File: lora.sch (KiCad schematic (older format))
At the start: 52 parts, among them J11 Conn_Coaxial, J2 Humidity, J3 Temp, J5 Temp, J6 VDD, J7 GPS, J8 SIM800, J9 I2C, Q1 AO3401A, Q2 AO3401A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

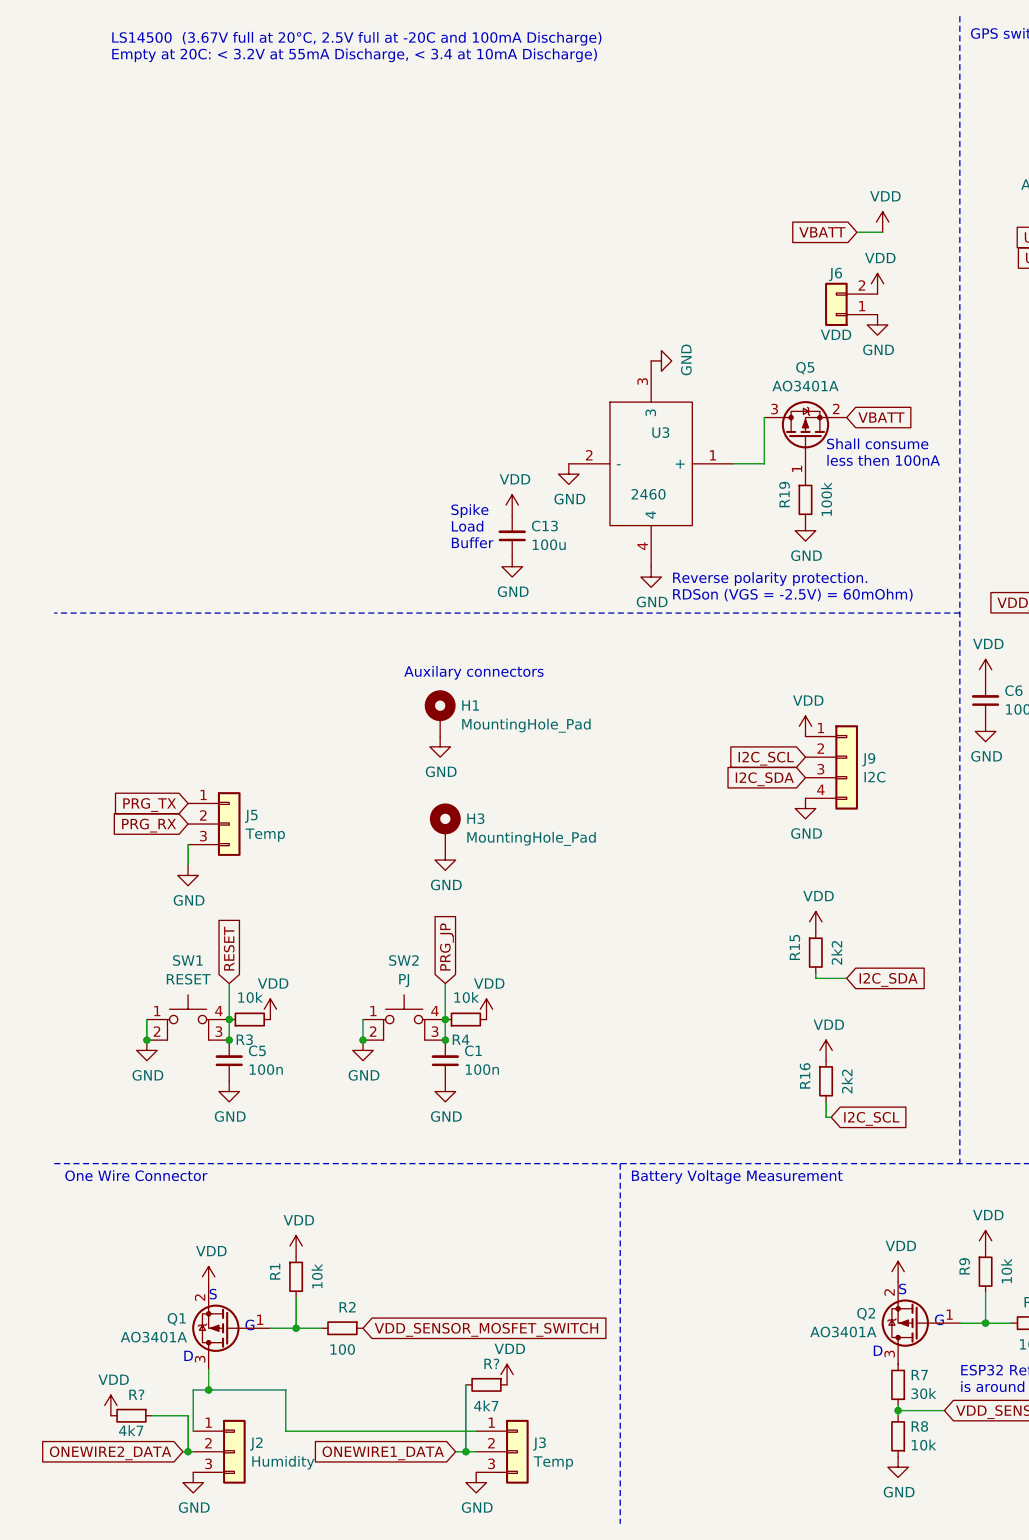
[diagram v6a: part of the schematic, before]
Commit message: updated part number step up
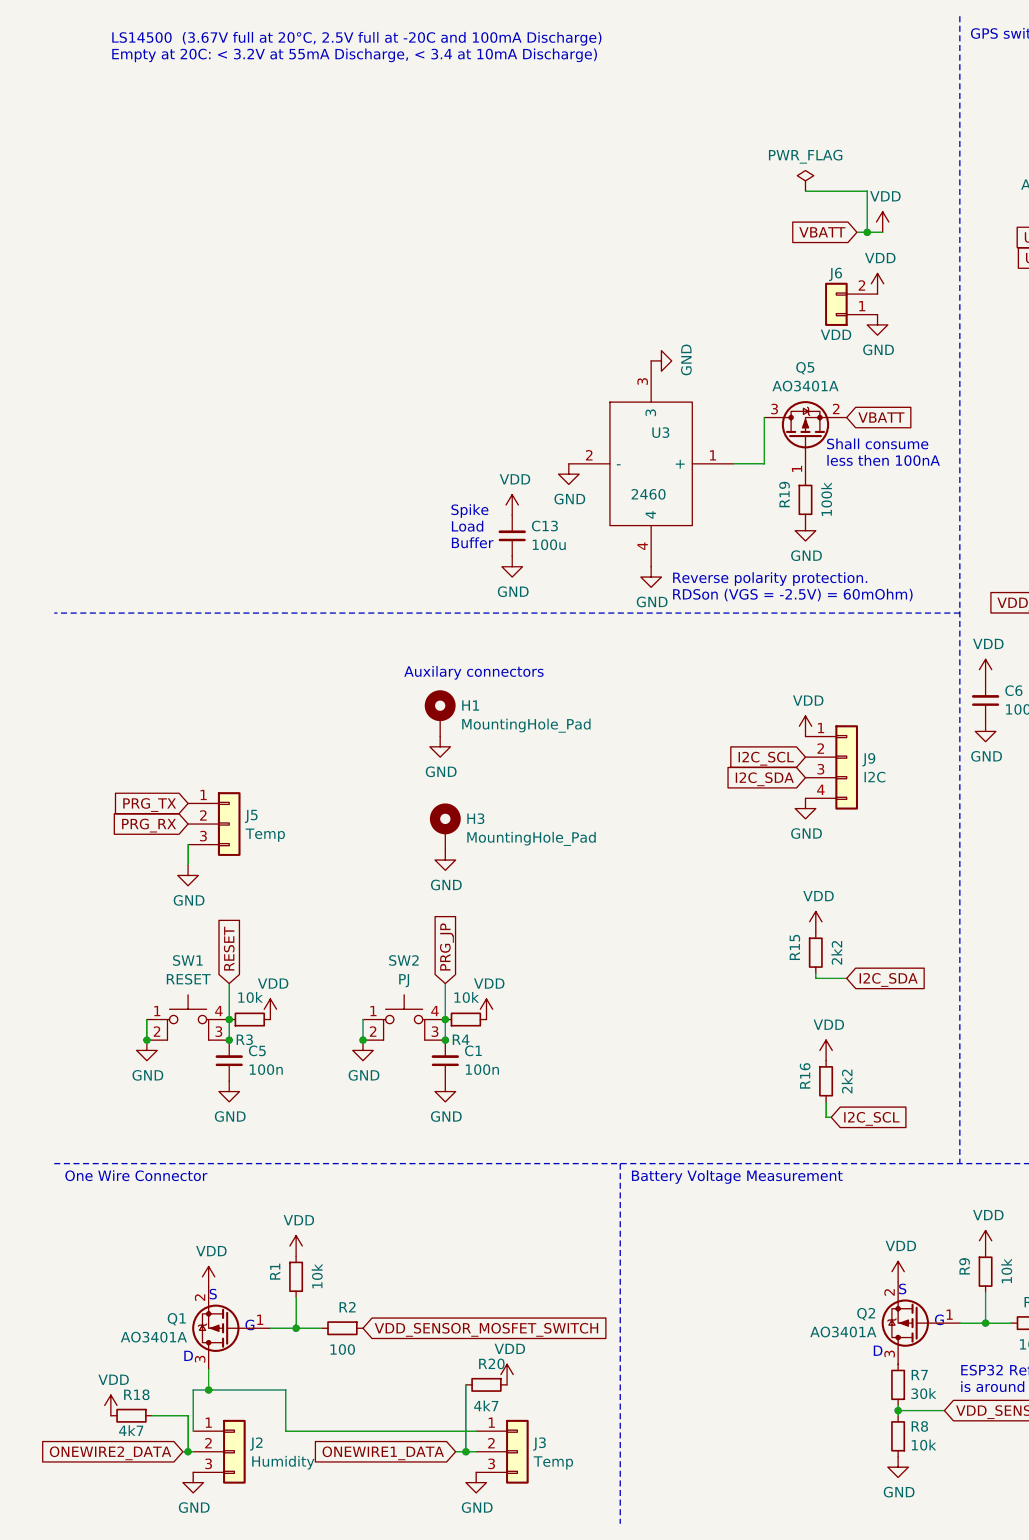
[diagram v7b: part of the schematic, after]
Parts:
- gave numbers to parts that had none: 2
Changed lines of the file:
@@
 $EndComp
 Wire Wire Line
-	4375 1525 4500 1525
+	4375 1525 4425 1525
 Wire Notes Line
 	3225 6050 3225 7800
@@
 	8350 3675 8550 3675
 $Comp
-L Device:R_Small R?
+L Device:R_Small R20
 U 1 1 614025B8
 P 2575 7125
-F 0 "R?" V 2475 7150 50  0000 C CNN
+F 0 "R20" V 2475 7150 50  0000 C CNN
 F 1 "4k7" V 2680 7125 50  0000 C CNN
 F 2 "Capacitor_SMD:C_0603_1608Metric" H 2575 7125 50  0001 C CNN
@@
 $EndComp
 $Comp
-L Device:R_Small R?
+L Device:R_Small R18
 U 1 1 61403C1F
 P 850 7275
-F 0 "R?" V 750 7300 50  0000 C CNN
+F 0 "R18" V 750 7300 50  0000 C CNN
 F 1 "4k7" V 925 7275 50  0000 C CNN
 F 2 "Capacitor_SMD:C_0603_1608Metric" H 850 7275 50  0001 C CNN
@@
 $EndComp
 $Comp
-L power:VDD #PWR?
+L power:VDD #PWR0141
 U 1 1 6140430D
 P 2675 7125
-F 0 "#PWR?" H 2675 6975 50  0001 C CNN
+F 0 "#PWR0141" H 2675 6975 50  0001 C CNN
 F 1 "VDD" H 2690 7298 50  0000 C CNN
 F 2 "" H 2675 7125 50  0001 C CNN
@@
 $EndComp
 $Comp
-L power:VDD #PWR?
+L power:VDD #PWR0142
 U 1 1 61405B69
 P 750 7275
-F 0 "#PWR?" H 750 7125 50  0001 C CNN
+F 0 "#PWR0142" H 750 7125 50  0001 C CNN
 F 1 "VDD" H 765 7448 50  0000 C CNN
 F 2 "" H 750 7275 50  0001 C CNN
@@
 	1125 7450 1100 7450
 NoConn ~ 6725 3725
+$Comp
+L power:PWR_FLAG #FLG0101
+U 1 1 61424CD0
+P 4125 1325
+F 0 "#FLG0101" H 4125 1400 50  0001 C CNN
+F 1 "PWR_FLAG" H 4125 1498 50  0000 C CNN
+F 2 "" H 4125 1325 50  0001 C CNN
+F 3 "~" H 4125 1325 50  0001 C CNN
+	1    4125 1325
+	1    0    0    -1
+$EndComp
+Wire Wire Line
+	4125 1325 4425 1325
+Wire Wire Line
+	4425 1325 4425 1525
+Connection ~ 4425 1525
+Wire Wire Line
+	4425 1525 4500 1525
 $EndSCHEMATC

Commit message: some steps done towards version 2. Progress recorded in hints.txt
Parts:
- removed J2: Humidity, Connector_PinHeader_2.54mm:PinHeader_1x03_P2.54mm_Horizontal, symbol Connector_Generic:Conn_01x03
- removed J8: SIM800, Connector_PinHeader_2.54mm:PinHeader_1x04_P2.54mm_Vertical, symbol Connector_Generic:Conn_01x04
- removed R18: 4k7, Capacitor_SMD:C_0603_1608Metric, symbol Device:R_Small
- added C?: 100n, Capacitor_SMD:C_0603_1608Metric, symbol Device:C_Small
- added JP?: ISense, symbol Jumper:SolderJumper_2_Bridged
- added R?: 10k, Capacitor_SMD:C_0603_1608Metric, symbol Device:R_Small
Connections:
- net UART1_TX is gone; now on net VDD_SENSE: U2.16 (IO13)
- net GND: now also C?.1
- net RFM_RST: now also R?.1
- net VDD: now also R?.2
- net VDD_SENSE: now also C?.2; no longer U2.4 (SENSOR_VP)
- net at U3.1 (+): now also JP?.1 (A); no longer Q5.3 (D)
- net GPS_MOSFET_SWITCH renamed 5V_ENABLE_SWITCH
- net 5V_ENABLE_SWITCH: now also R10.1, R2.1
- net ONEWIRE2_DATA renamed EXT_ADC_SENSE2
- net UART1_RX renamed EXT_ADC_SENSE
- net VDD_SENSE_MOSFET_SWITCH: no longer names the net of U2.6 (IO34)
- net VDD_SENSE_MOSFET_SWITCH: no longer R10.1
- net VDD_SENSOR_MOSFET_SWITCH: no longer names the net of U2.7 (IO35)
- net VDD_SENSOR_MOSFET_SWITCH: no longer R2.1
- new net: JP?.2 (B), Q5.3 (D)
- no-connect marks 14 -> 17
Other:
- note removed: "Cellular Network"
- note removed: "GPS switchable"
- note removed: "SIM800 requires up to 2A in \nburst mode and 3.4V to 4.4V"
- note removed: "UBLOX Neo 6: 2.7 - 3.6V"
- note removed: "Works properly above 2.5V VDD!"
- moved on the sheet: Q5, R19
